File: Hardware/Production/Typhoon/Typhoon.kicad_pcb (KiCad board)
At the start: 4 copper layers, 95 parts, among them IC1 TMC2209-LA, J1 RBUS, J2 USB_C_Receptacle_USB2.0, J3 Motor Breakout, J4 GPIO Breakout, J9 Conn_01x01_Socket, U1 ESP32-S3, U2 SN65HVD230, U3 LM66200DRLR, U4 MAX77827AEFD+T, U5 SC4215ASTRT, U7 XL1509-3.3, Y1 R940000171

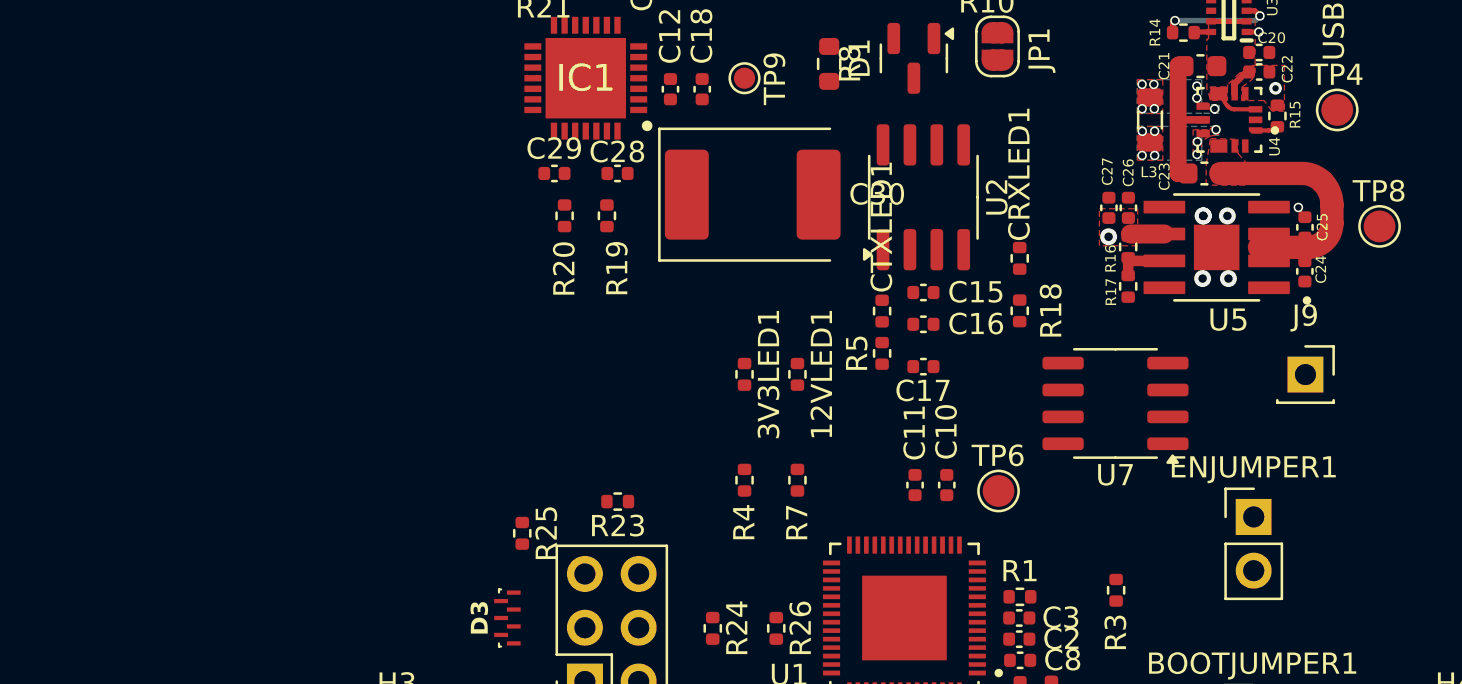
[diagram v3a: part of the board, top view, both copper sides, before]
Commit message: Updated schematic, added mosfets to ENN and SPREAD pins of TMC2209 and connected INDEX, CLK, and VREF to GPIO pins
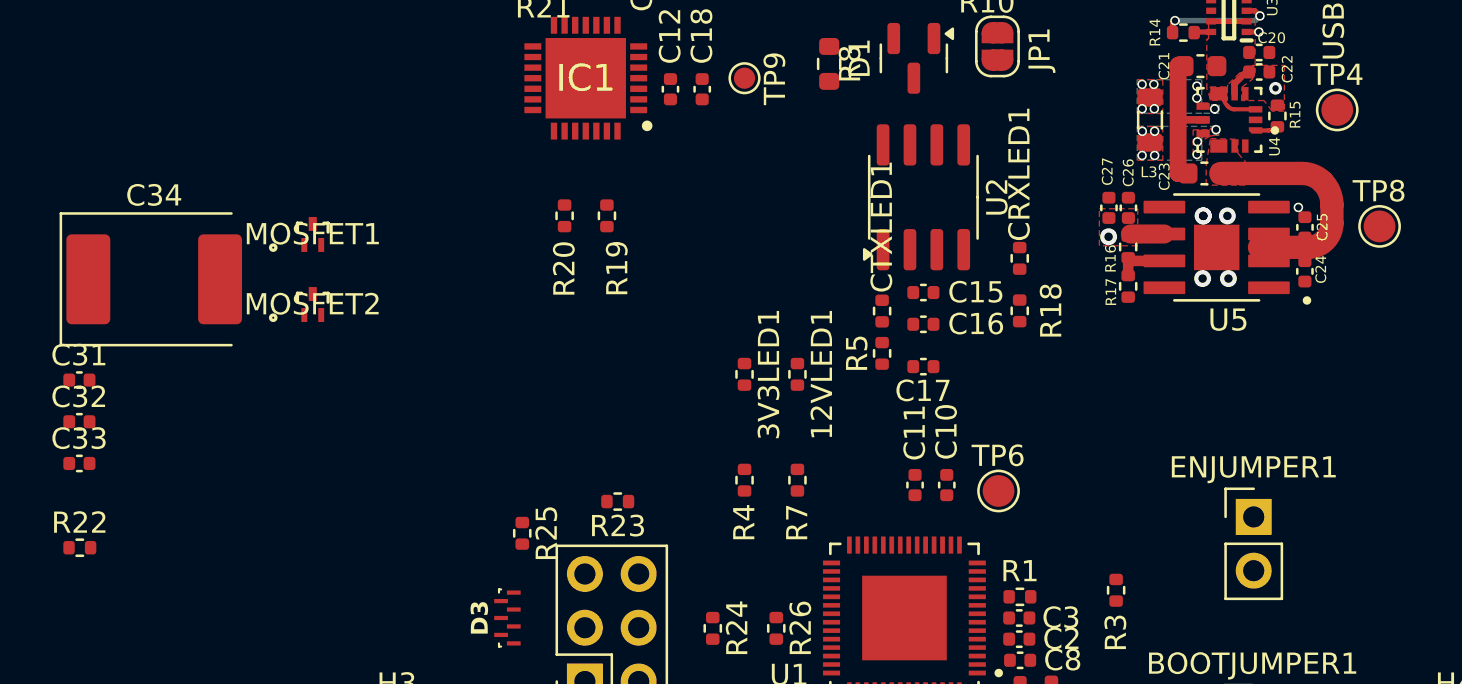
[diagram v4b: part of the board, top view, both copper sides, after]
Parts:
- removed C28, C29: 100n, Capacitor_SMD:C_0402_1005Metric
- removed C30: 100u, Capacitor_Tantalum_SMD:CP_EIA-7360-38_Kemet-E
- removed J9: Conn_01x01_Socket, Connector_PinSocket_2.54mm:PinSocket_1x01_P2.54mm_Vertical
- removed U7: XL1509-3.3, Package_SO:SOIC-8_3.9x4.9mm_P1.27mm
- added C31: 100nF, Capacitor_SMD:C_0402_1005Metric, F.Cu at (87.0, 93.8)
- added C32: 100nF, Capacitor_SMD:C_0402_1005Metric, F.Cu at (87.0, 95.8)
- added C33: 100nF, Capacitor_SMD:C_0402_1005Metric, F.Cu at (87.0, 97.8)
- added C34: 100uF, Capacitor_Tantalum_SMD:CP_EIA-7360-38_Kemet-E, F.Cu at (90.5, 89.1)
- added MOSFET1: SSM3K15AMFV, SSM3K15AMFV:VESM_TOS, F.Cu at (98.0, 87.0)
- added MOSFET2: SSM3K15AMFV, SSM3K15AMFV:VESM_TOS, F.Cu at (98.0, 90.3)
- added R22: 50, Resistor_SMD:R_0402_1005Metric, F.Cu at (87.0, 101.8)
- C12: value 22n -> 22nF
- C18: value 100n -> 4.7uF
- C19: value 2.2u -> 2.2uF
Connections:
- C18 pad 1: +16.8V -> Net-(IC1-5VOUT)
- C18 pad 2: Net-(IC1-VCP) -> GND
- IC1 pad 12: unconnected-(IC1-INDEX-Pad12) -> /INDEX
- IC1 pad 13: unconnected-(IC1-CLK-Pad13) -> /EXT_CLK
- IC1 pad 17: unconnected-(IC1-VREF-Pad17) -> /VREF
- IC1 pad 2: GND -> Net-(IC1-ENN)
- IC1 pad 7: unconnected-(IC1-SPREAD-Pad7) -> Net-(IC1-SPREAD)
- U1 pad 23: unconnected-(U1-GPIO17/ADC2_CH6/DAC_2-Pad23) -> /INDEX
- U1 pad 24: unconnected-(U1-GPIO18/ADC2_CH7/DAC_1-Pad24) -> /VREF
- U1 pad 27: unconnected-(U1-GPIO21-Pad27) -> Net-(U1-GPIO21)
- U1 pad 36: unconnected-(U1-SPICLK_N/GPIO48-Pad36) -> /EN
- U1 pad 37: unconnected-(U1-SPICLK_P/GPIO47-Pad37) -> /SPREAD_EN

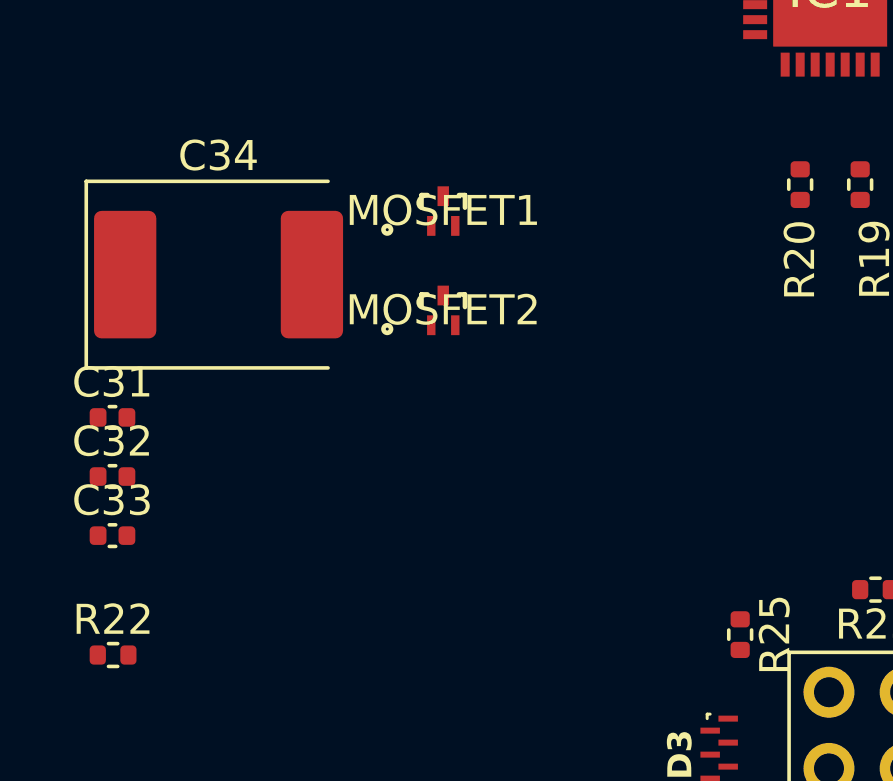
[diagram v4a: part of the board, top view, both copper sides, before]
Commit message: Small fixes to some footprints and used a different model for NMOS transistors
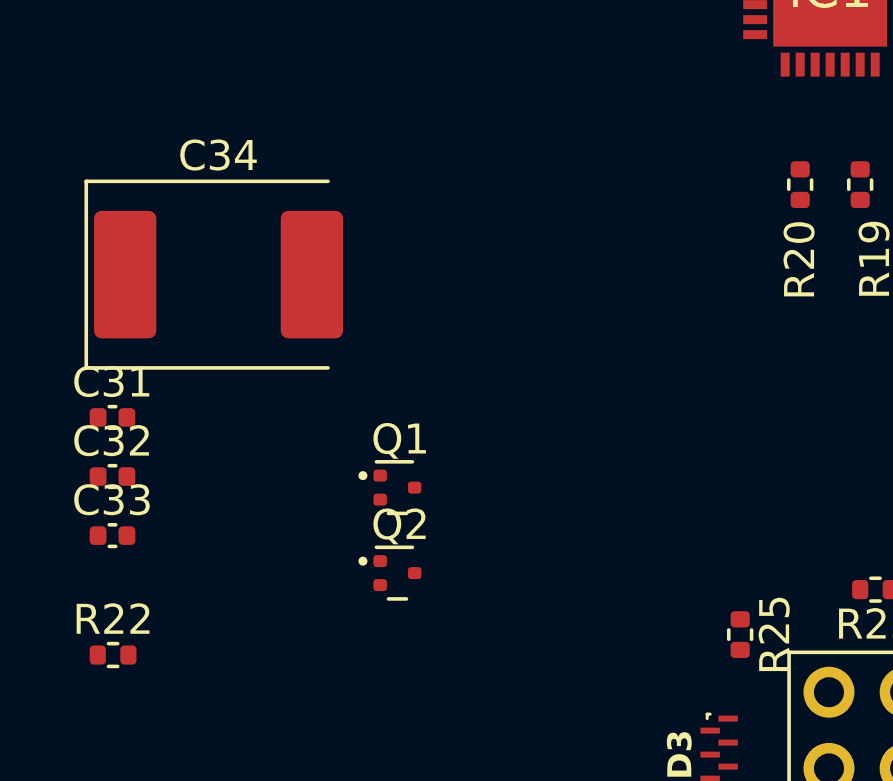
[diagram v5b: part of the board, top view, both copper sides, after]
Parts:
- removed MOSFET1, MOSFET2: SSM3K15AMFV, SSM3K15AMFV:VESM_TOS
- added Q1: SPREAD_NMOS, iclr:SOT-723, F.Cu at (96.5, 96.2)
- added Q2: ENN_NMOS, iclr:SOT-723, F.Cu at (96.5, 99.0)

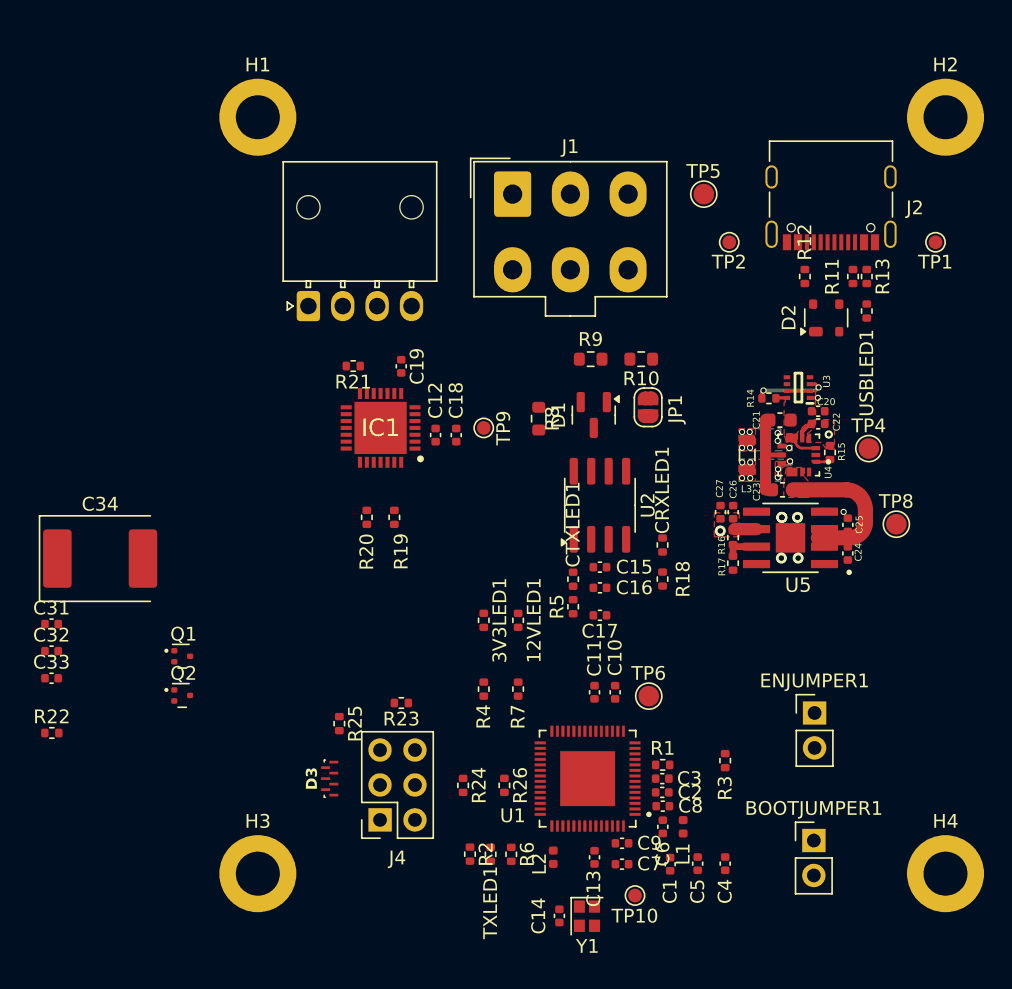
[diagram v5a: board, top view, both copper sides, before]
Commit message: Updated layout
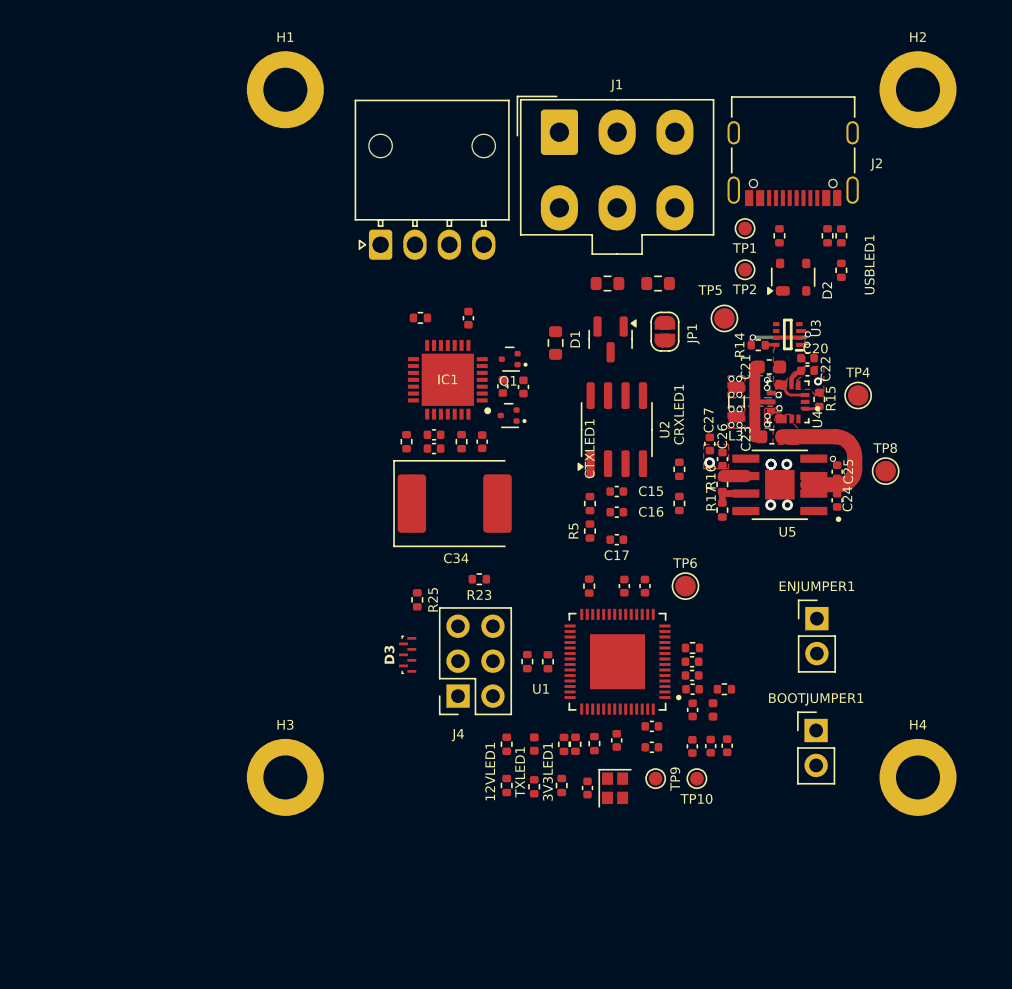
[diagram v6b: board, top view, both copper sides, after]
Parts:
- moved R22 40.5 mm to (126.1, 91.1), turned to 90 degrees
- moved C33 35.7 mm to (118.3, 80.6), turned to 90 degrees
- moved Q1 32.1 mm to (120.3, 74.6), turned to 180 degrees
- moved C32 31.5 mm to (114.8, 81.1)
- moved Q2 31.3 mm to (120.2, 78.7), turned to 180 degrees
- moved C31 31.0 mm to (114.8, 80.1)
- moved TP9 28.4 mm to (130.9, 105.1)
- moved C34 26.1 mm to (116.3, 85.1)
- moved TP1 13.9 mm to (137.4, 65.1)
- moved 3V3LED1 13.3 mm to (124.1, 105.6), turned to 90 degrees
- moved 12VLED1 12.0 mm to (120.1, 105.6), turned to 90 degrees
- moved D3 10.6 mm to (112.9, 96.1)
- moved J4 10.6 mm to (116.6, 99.1)
- moved R23 10.6 mm to (118.1, 90.6)
- moved R25 10.6 mm to (113.6, 92.1)
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- renumbered C14 to Ce, C18 to Ce, C6 to Ce, R13 to Re
